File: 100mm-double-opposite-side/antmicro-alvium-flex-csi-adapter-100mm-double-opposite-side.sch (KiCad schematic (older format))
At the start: 4 parts, among them J1 WE_687622100002_FLEX, J2 WE_687622100002_FLEX, J3 WE_687650100002_FLEX

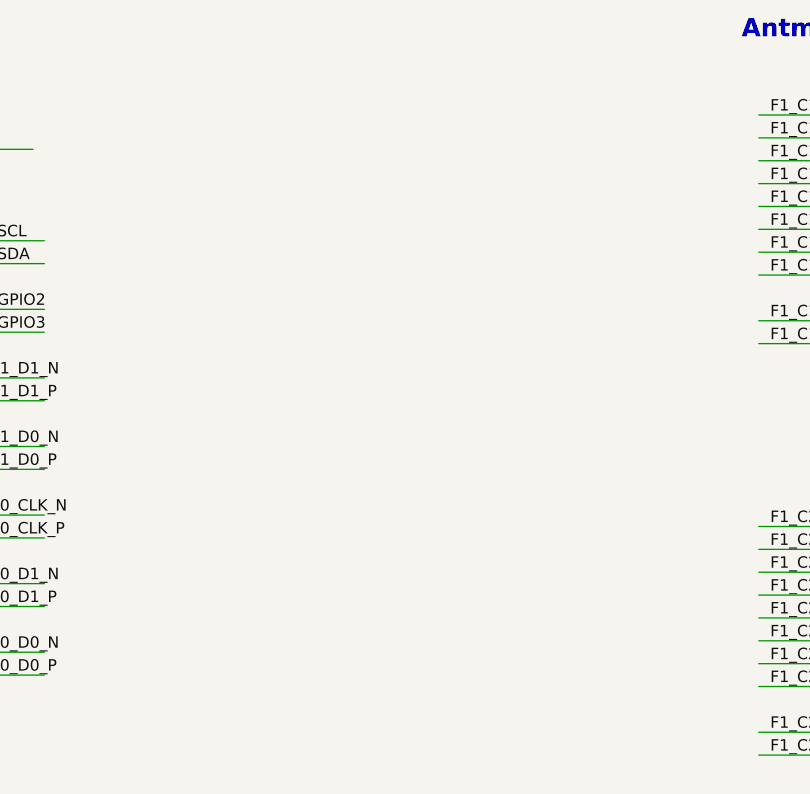
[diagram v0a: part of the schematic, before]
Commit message: Add NMOS transistors for camera triggering in 100mm double opposite side variant
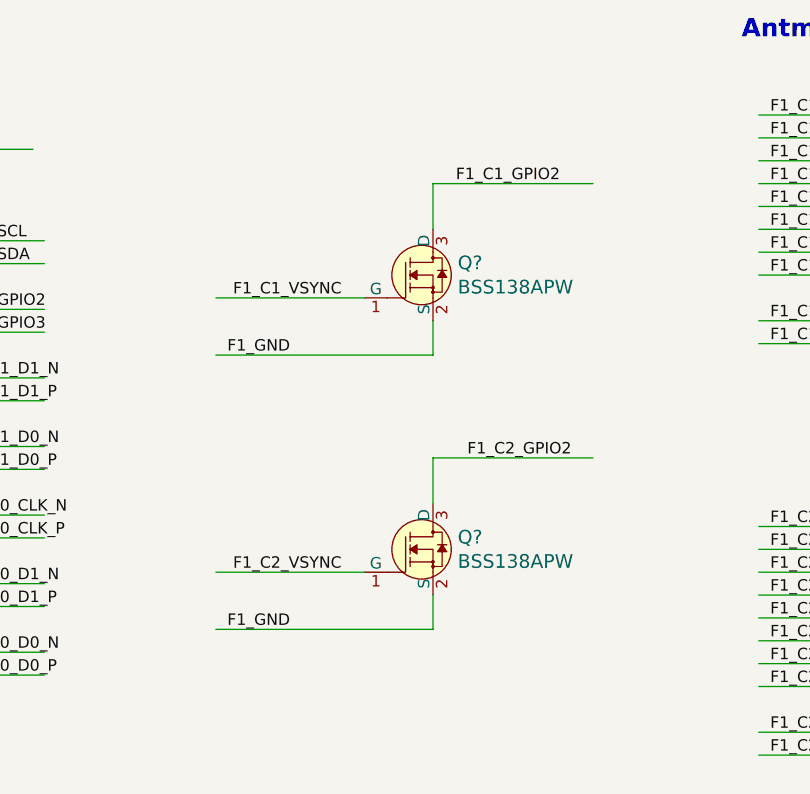
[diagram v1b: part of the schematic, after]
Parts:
- added Q? (x2): BSS138APW, antmicro-alvium-flex-csi-adapter-footprints:SC70-3, symbol antmicro-alvium-flex-csi-adapter:BSS138APW
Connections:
- wire segments 111 -> 121
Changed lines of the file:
@@
 EndData
 $EndBitmap
+$Comp
+L antmicro-alvium-flex-csi-adapter:BSS138APW Q?
+U 1 1 5F898D59
+P 8300 3750
+F 0 "Q?" H 8408 3803 60  0000 L CNN
+F 1 "BSS138APW" H 8408 3697 60  0000 L CNN
+F 2 "antmicro-alvium-flex-csi-adapter-footprints:SC70-3" H 8500 3950 60  0001 L CNN
+F 3 "" H 8500 4050 60  0001 L CNN
+F 4 "BSS138PW" H 8500 4250 60  0001 L CNN "MPN"
+F 5 "ON Semiconductor" H 8500 4850 60  0001 L CNN "Manufacturer"
+	1    8300 3750
+	1    0    0    -1
+$EndComp
+Text Label 7400 4100 0    50   ~ 0
+F1_GND
+Text Label 7900 3850 2    50   ~ 0
+F1_C1_VSYNC
+Wire Wire Line
+	8000 3850 7350 3850
+Wire Wire Line
+	8300 3950 8300 4100
+Wire Wire Line
+	8300 4100 7350 4100
+Wire Wire Line
+	8300 3550 8300 3350
+Wire Wire Line
+	8300 3350 9000 3350
+Text Label 8400 3350 0    50   ~ 0
+F1_C1_GPIO2
+$Comp
+L antmicro-alvium-flex-csi-adapter:BSS138APW Q?
+U 1 1 5F8B8E2D
+P 8300 4950
+F 0 "Q?" H 8408 5003 60  0000 L CNN
+F 1 "BSS138APW" H 8408 4897 60  0000 L CNN
+F 2 "antmicro-alvium-flex-csi-adapter-footprints:SC70-3" H 8500 5150 60  0001 L CNN
+F 3 "" H 8500 5250 60  0001 L CNN
+F 4 "BSS138PW" H 8500 5450 60  0001 L CNN "MPN"
+F 5 "ON Semiconductor" H 8500 6050 60  0001 L CNN "Manufacturer"
+	1    8300 4950
+	1    0    0    -1
+$EndComp
+Wire Wire Line
+	8000 5050 7350 5050
+Wire Wire Line
+	8300 5150 8300 5300
+Wire Wire Line
+	8300 5300 7350 5300
+Wire Wire Line
+	8300 4750 8300 4550
+Wire Wire Line
+	8300 4550 9000 4550
+Text Label 7900 5050 2    50   ~ 0
+F1_C2_VSYNC
+Text Label 7400 5300 0    50   ~ 0
+F1_GND
+Text Label 8450 4550 0    50   ~ 0
+F1_C2_GPIO2
 $EndSCHEMATC

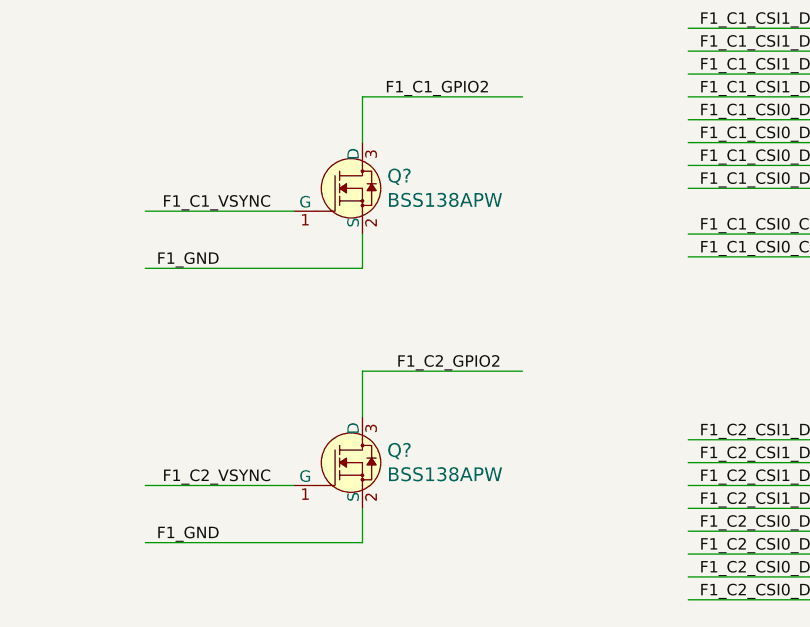
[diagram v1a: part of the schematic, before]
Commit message: Add NMOS transistors for camera triggering in 100mm double same side variant
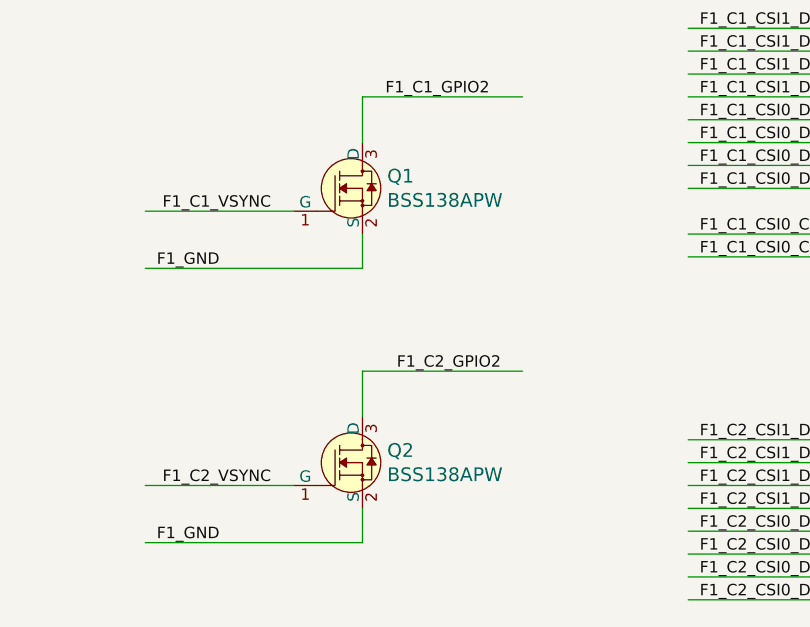
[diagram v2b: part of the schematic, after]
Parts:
- gave numbers to parts that had none: 2
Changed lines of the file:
@@
 $EndBitmap
 $Comp
-L antmicro-alvium-flex-csi-adapter:BSS138APW Q?
+L antmicro-alvium-flex-csi-adapter:BSS138APW Q1
 U 1 1 5F898D59
 P 8300 3750
-F 0 "Q?" H 8408 3803 60  0000 L CNN
+F 0 "Q1" H 8408 3803 60  0000 L CNN
 F 1 "BSS138APW" H 8408 3697 60  0000 L CNN
 F 2 "antmicro-alvium-flex-csi-adapter-footprints:SC70-3" H 8500 3950 60  0001 L CNN
@@
 F1_C1_GPIO2
 $Comp
-L antmicro-alvium-flex-csi-adapter:BSS138APW Q?
+L antmicro-alvium-flex-csi-adapter:BSS138APW Q2
 U 1 1 5F8B8E2D
 P 8300 4950
-F 0 "Q?" H 8408 5003 60  0000 L CNN
+F 0 "Q2" H 8408 5003 60  0000 L CNN
 F 1 "BSS138APW" H 8408 4897 60  0000 L CNN
 F 2 "antmicro-alvium-flex-csi-adapter-footprints:SC70-3" H 8500 5150 60  0001 L CNN
